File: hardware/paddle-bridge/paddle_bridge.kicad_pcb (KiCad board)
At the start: 2 copper layers, 47.5 x 40 mm, 15 parts, among them J1 APOLLO (P4 header GND,52,51,5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, J2 MACHINE: paddle pair + Micra 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, U1 AQY212EH, U2 LH1502BB, U3 LH1502BB

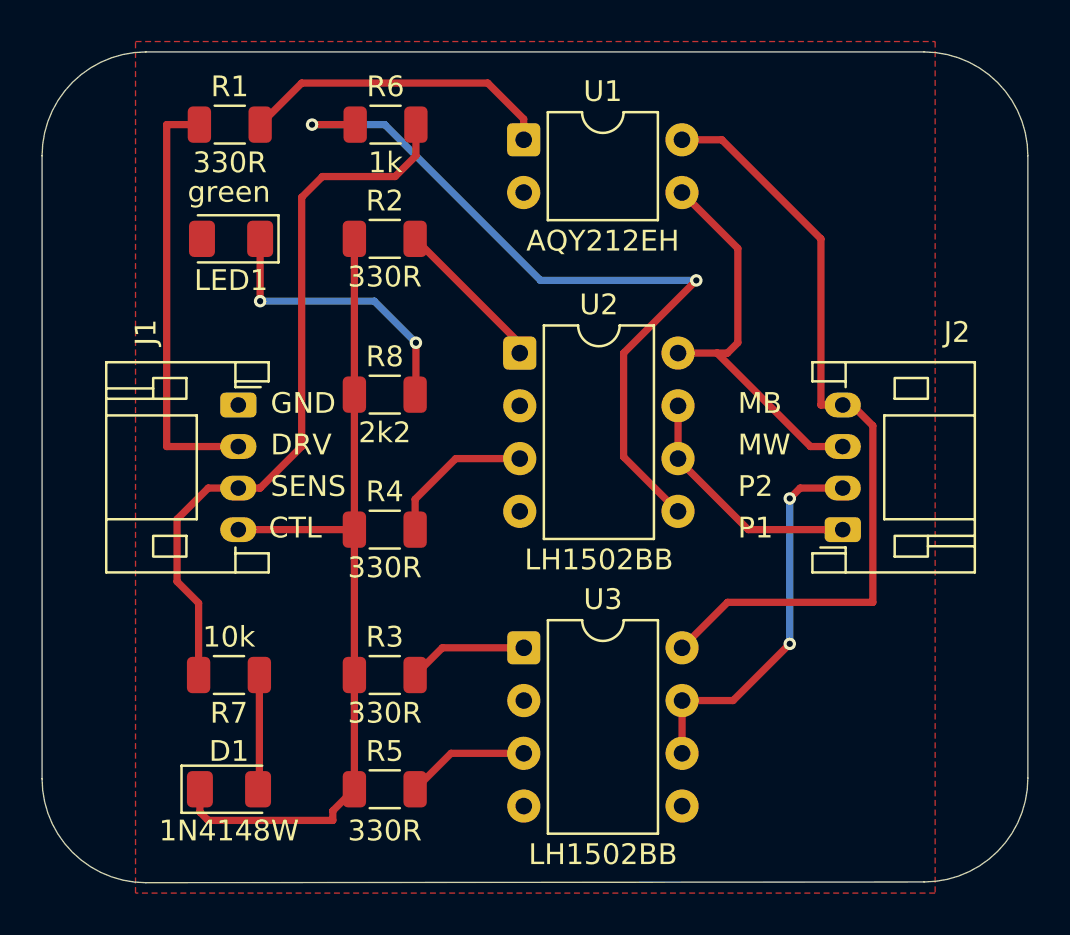
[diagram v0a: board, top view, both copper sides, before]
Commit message: hardware: Apollo Link layout - pull the GND pour back to the IC centre line
Keeps every Micra-side pin (U1 3/4, U2/U3 pins 8-5) clear of remote-domain
copper; U3 pin 5's ground return is a track instead of pour. DRC clean.
Regenerated gerbers/drill zip to match.
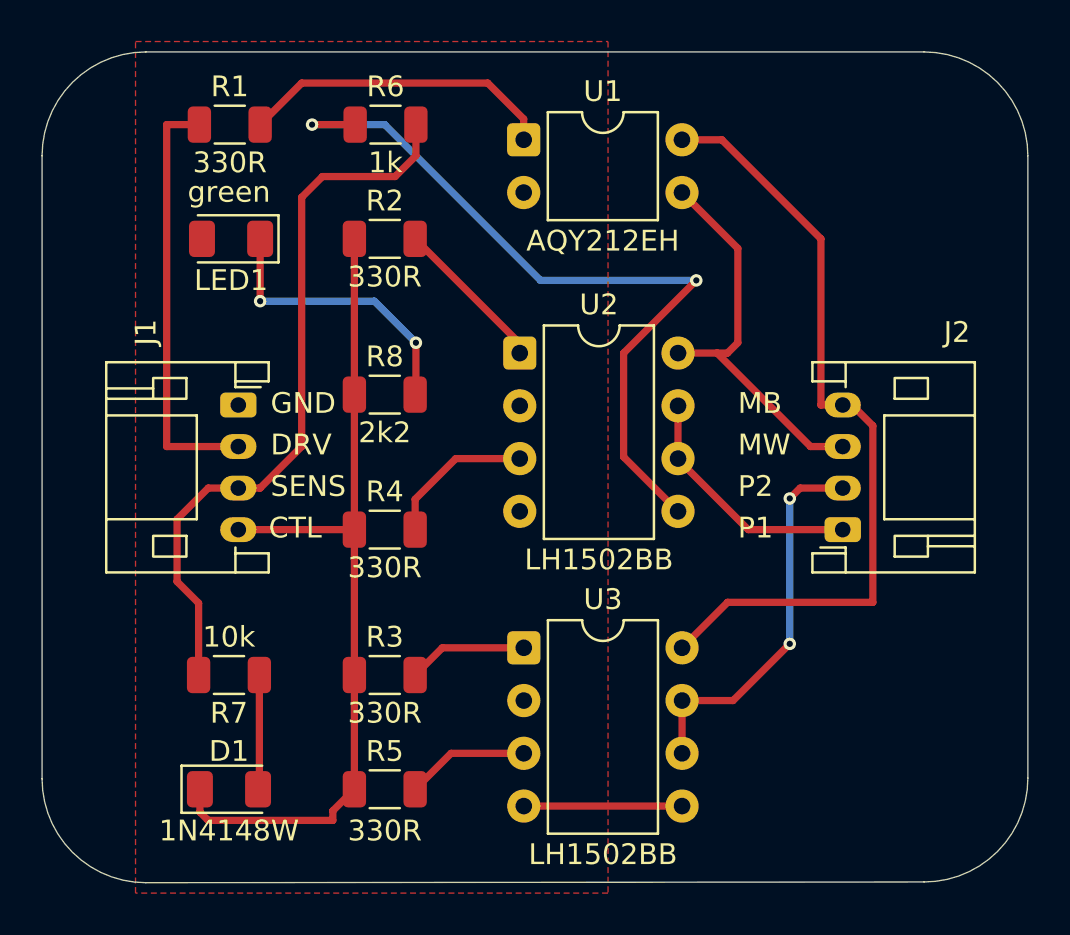
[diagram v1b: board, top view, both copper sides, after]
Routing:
- net /GND_R: track 0.00 -> 7.62 mm
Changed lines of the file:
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@@
+	)
+	(segment
+		(start 149.315 96.31)
+		(end 141.695 96.31)
+		(width 0.35)
+		(layer "F.Cu")
+		(net "/GND_R")
 	)
 	(segment
@@
 		(polygon
 			(pts
-				(xy 123 59.5) (xy 161.5 59.5) (xy 161.5 100.5) (xy 123 100.5)
+				(xy 123 59.5) (xy 145.75 59.5) (xy 145.75 100.5) (xy 123 100.5)
 			)
 		)
